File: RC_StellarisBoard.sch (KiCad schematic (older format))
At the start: 46 parts, among them K1 CONN_3, K2 CONN_3, K3 CONN_3, K4 CONN_3, K5 CONN_3, P1 CONN_2, P2 CONN_1, P3 CONN_1, P4 CONN_1, P5 CONN_1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

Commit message: buck boost, DCDC 5 done, servos done
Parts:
- removed D1: ZENER, ~, symbol ZENER
- removed Q1: MOSFET_P, ~, symbol MOSFET_P
- removed U3: NCP1117ST12T3G, ~, symbol NCP1117ST12T3G
- added C7: 22uF, ~, symbol C
- added L2: 2.2uH, ~, symbol INDUCTOR_SMALL
- added Q1: MOS_N, symbol MOS_N
- added R19: shunt, symbol R
- added U3: LM3668_DQB_12_SDF12A, symbol LM3668_DQB_12_SDF12A
- C4: value 1uF -> 10uF
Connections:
- wire segments 111 -> 122
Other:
- moved on the sheet: C4, R9

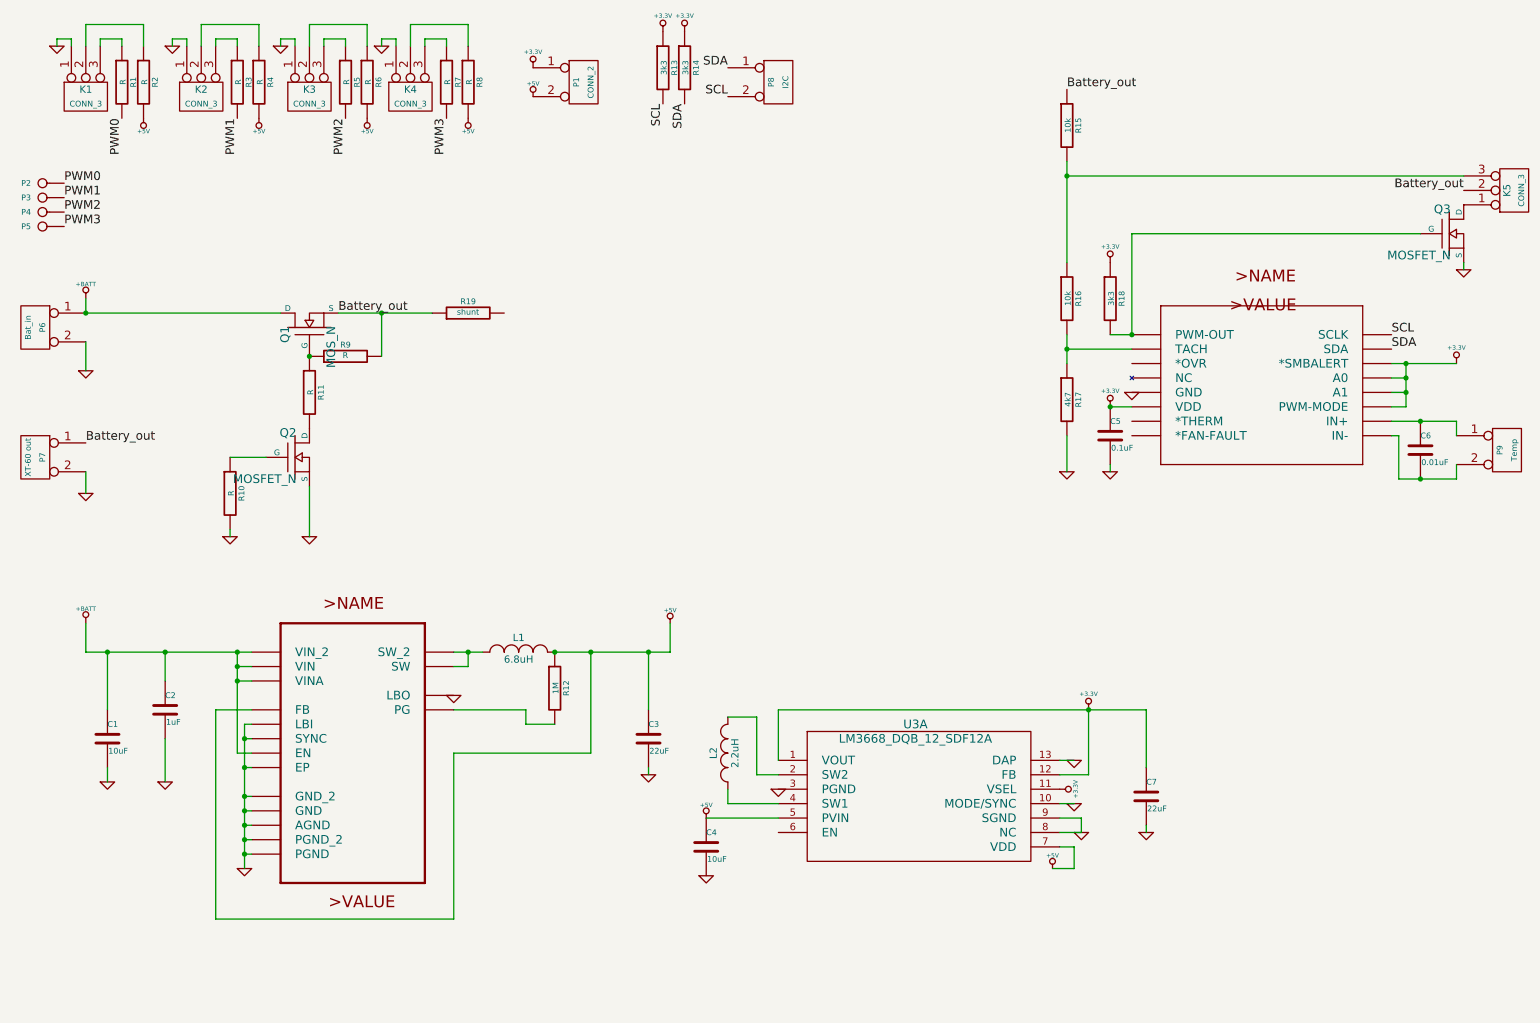
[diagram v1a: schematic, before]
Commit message: boost, mosfet + shunt
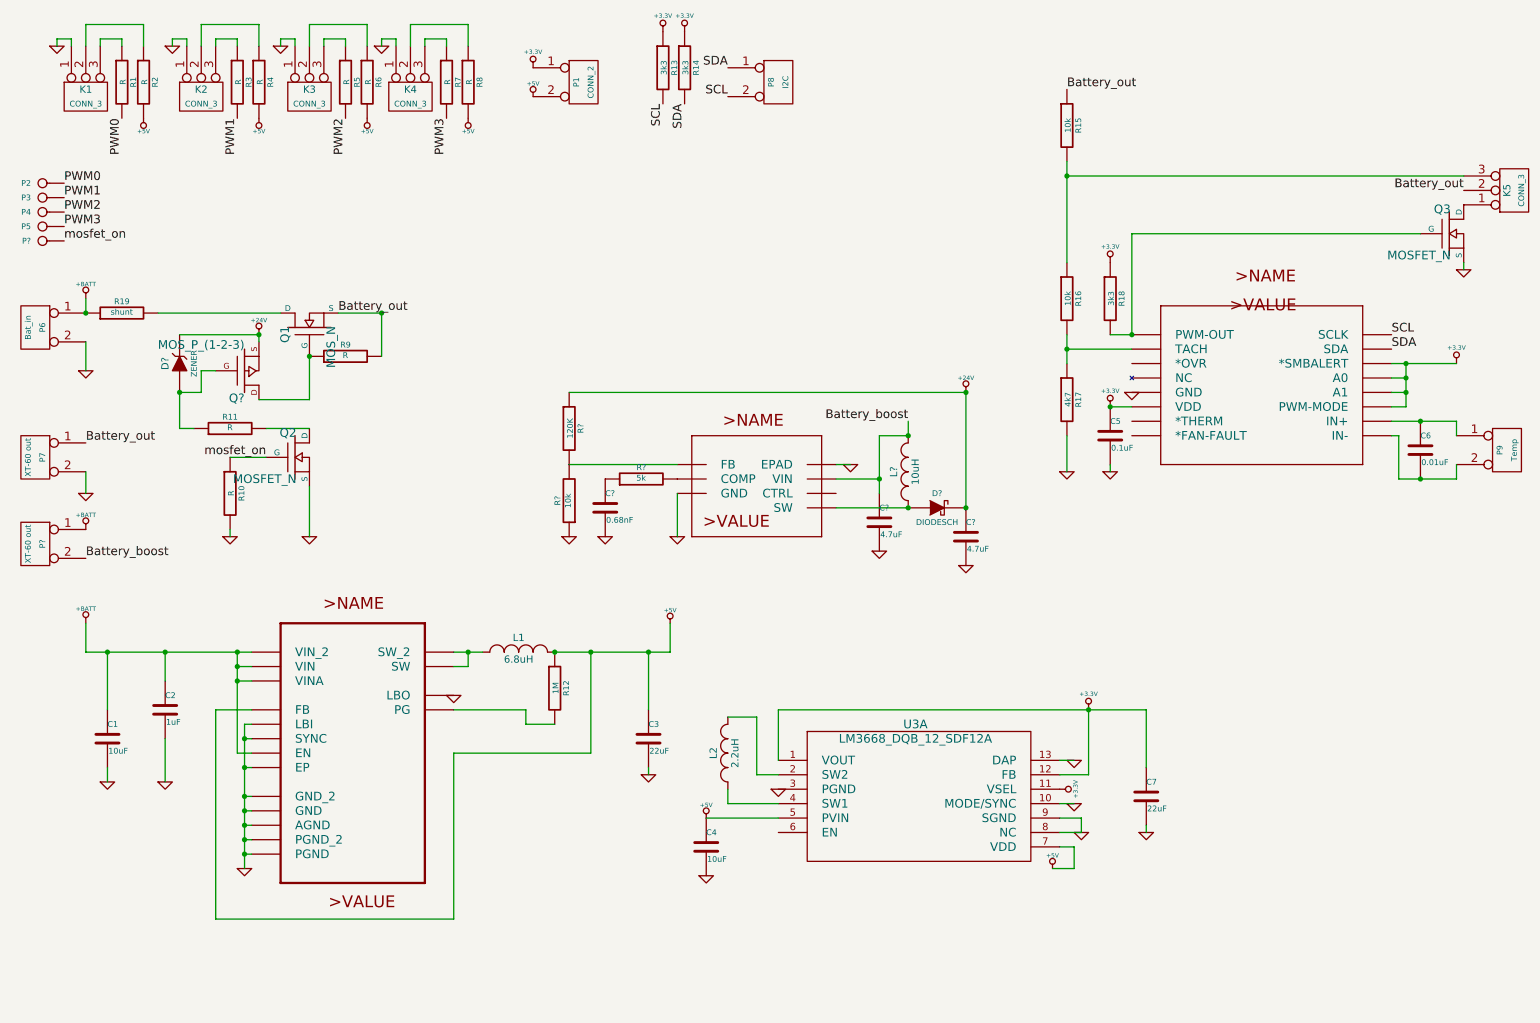
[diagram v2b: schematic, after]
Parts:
- added C?: 0.68nF, ~, symbol C
- added C? (x2): 4.7uF, ~, symbol C
- added D?: DIODESCH, ~, symbol DIODESCH
- added D?: ZENER, ~, symbol ZENER
- added L?: 10uH, ~, symbol INDUCTOR_SMALL
- added P?: XT-60 out, symbol CONN_2
- added P?: CONN_1, symbol CONN_1
- added Q?: MOS_P_(1-2-3), symbol MOS_P_(1-2-3)
- added R?: 5k, ~, symbol R
- added R?: 10k, ~, symbol R
- added R?: 120K, ~, symbol R
- added U?: TPS61170_DRV_6_DRV6_1P6X1, symbol TPS61170_DRV_6_DRV6_1P6X1
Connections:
- net +BATT: now also R19.1, P?.1 (P1); no longer Q1.D
- net Battery_out: no longer R19.1
- net GND: now also C?.2, C?.2, C?.2, R?.1, U?.3 (GND), U?.7 (EPAD)
- net mosfet_on: now reaches Q2.G, R10.1
- net mosfet_on: now also P?.1
- net at Q1.G, R9.1: now also Q?.D; no longer R11.1
- net at R19.2: now also Q1.D
- new net: D?.1 (A), Q?.G, R11.1
- new net: R?.2, R?.2, U?.1 (FB)
- new net: R?.2, U?.2 (COMP)
- new net: D?.1 (A), L?.1, U?.4 (SW)
- new net: C?.1, R?.1
- new net +24V: C?.1, D?.2 (K), D?.2 (K), Q?.S, R?.1
- new net Battery_boost: C?.1, L?.2, P?.2 (PM), U?.6 (VIN)
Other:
- moved on the sheet: R11, R19

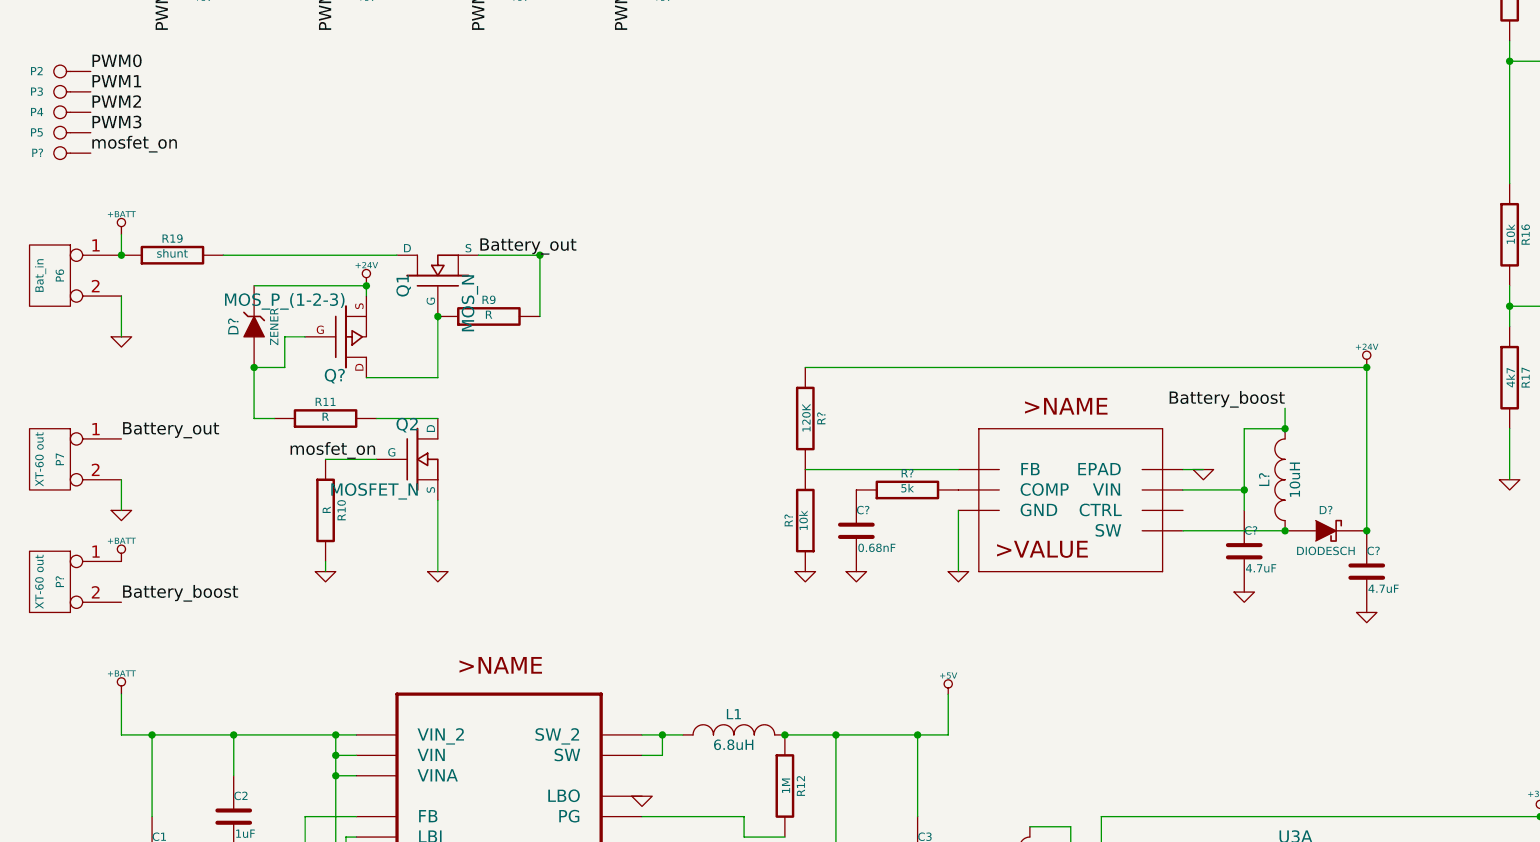
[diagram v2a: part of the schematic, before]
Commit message: falta footprints diodo
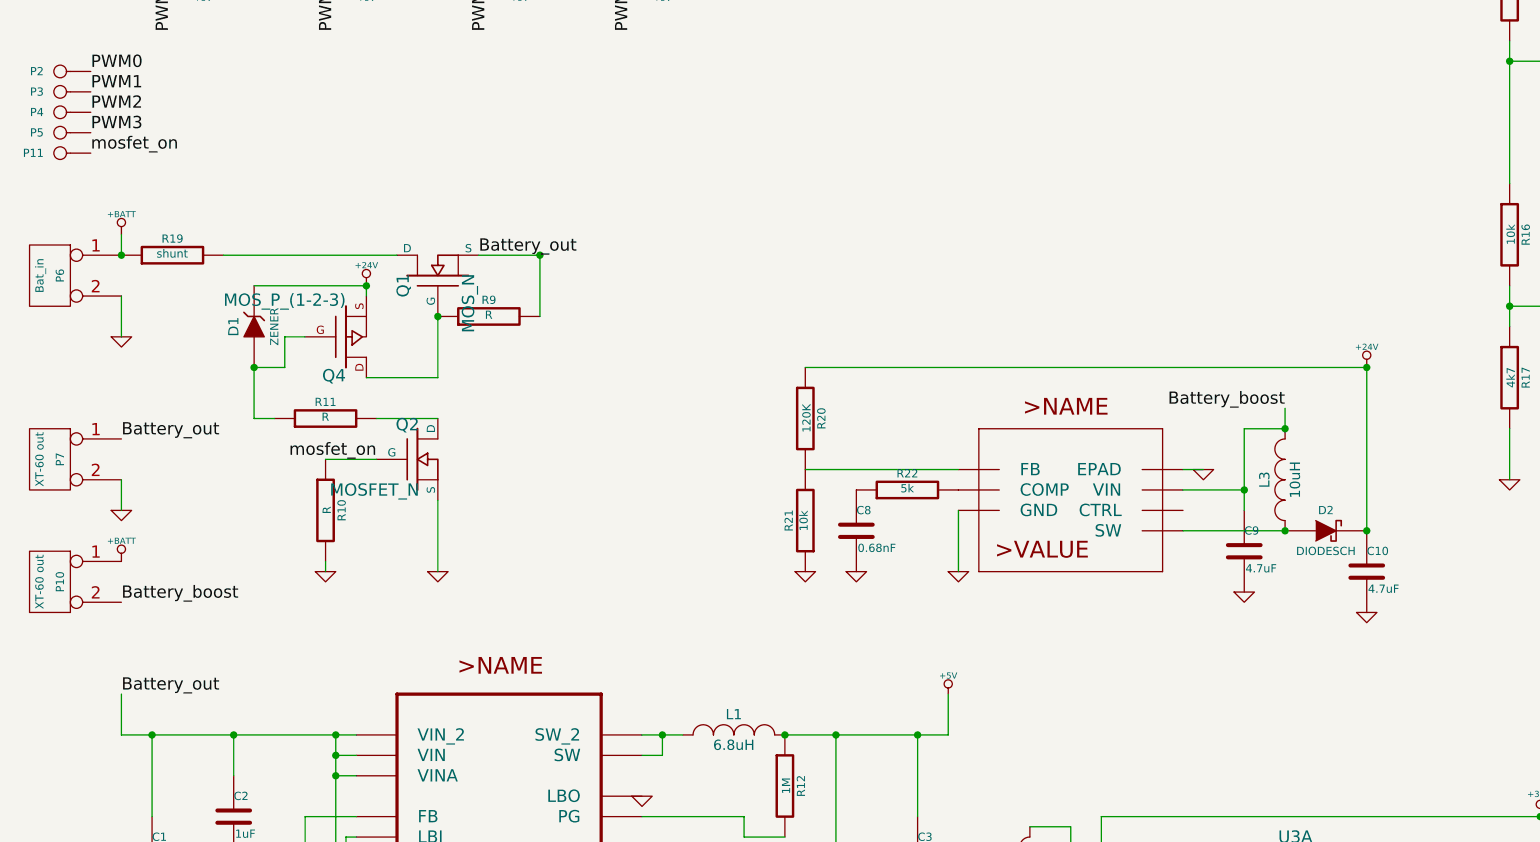
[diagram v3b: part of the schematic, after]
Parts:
- gave numbers to parts that had none: 13
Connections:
- net +BATT: no longer C1.1, C2.1, U2.2 (VIN_2), U2.3 (VIN), U2.4 (EN), U2.8 (VINA)
- net Battery_out: now also C1.1, C2.1, U2.2 (VIN_2), U2.3 (VIN), U2.4 (EN), U2.8 (VINA)
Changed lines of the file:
@@
 Sheet 1 1
 Title ""
-Date "6 jan 2014"
+Date "7 jan 2014"
 Rev ""
 Comp ""
@@
 	1100 2600 1100 2500
 Connection ~ 1100 2600
-$Comp
-L +BATT #PWR014
-U 1 1 52C981E3
-P 1100 4750
-F 0 "#PWR014" H 1100 4700 20  0001 C CNN
-F 1 "+BATT" H 1100 4850 30  0000 C CNN
-F 2 "" H 1100 4750 60  0000 C CNN
-F 3 "" H 1100 4750 60  0000 C CNN
-	1    1100 4750
-	1    0    0    -1
-$EndComp
 Wire Wire Line
 	1100 4750 1100 4950
@@
 $EndComp
 $Comp
-L TPS61170_DRV_6_DRV6_1P6X1 U?
+L TPS61170_DRV_6_DRV6_1P6X1 U4
 U 1 1 52CB3E20
 P 5700 3750
-F 0 "U?" H 5700 3750 0   0001 C CNN
+F 0 "U4" H 5700 3750 0   0001 C CNN
 F 1 "TPS61170_DRV_6_DRV6_1P6X1" H 5700 3750 0   0001 C CNN
 F 2 "" H 5700 3750 60  0000 C CNN
@@
 $EndComp
 $Comp
-L R R?
+L R R22
 U 1 1 52CB3E37
 P 4950 3750
-F 0 "R?" V 5030 3750 40  0000 C CNN
+F 0 "R22" V 5030 3750 40  0000 C CNN
 F 1 "5k" V 4957 3751 40  0000 C CNN
 F 2 "~" V 4880 3750 30  0000 C CNN
@@
 $EndComp
 $Comp
-L C C?
+L C C8
 U 1 1 52CB3E3D
 P 4700 3950
-F 0 "C?" H 4700 4050 40  0000 L CNN
+F 0 "C8" H 4700 4050 40  0000 L CNN
 F 1 "0.68nF" H 4706 3865 40  0000 L CNN
 F 2 "~" H 4738 3800 30  0000 C CNN
@@
 $EndComp
 $Comp
-L GND #PWR?
+L GND #PWR042
 U 1 1 52CB3E43
 P 4700 4150
-F 0 "#PWR?" H 4700 4150 30  0001 C CNN
+F 0 "#PWR042" H 4700 4150 30  0001 C CNN
 F 1 "GND" H 4700 4080 30  0001 C CNN
 F 2 "" H 4700 4150 60  0000 C CNN
@@
 $EndComp
 $Comp
-L GND #PWR?
+L GND #PWR043
 U 1 1 52CB3E49
 P 5200 4150
-F 0 "#PWR?" H 5200 4150 30  0001 C CNN
+F 0 "#PWR043" H 5200 4150 30  0001 C CNN
 F 1 "GND" H 5200 4080 30  0001 C CNN
 F 2 "" H 5200 4150 60  0000 C CNN
@@
 	5200 4150 5200 3850
 $Comp
-L R R?
+L R R21
 U 1 1 52CB3F80
 P 4450 3900
-F 0 "R?" V 4530 3900 40  0000 C CNN
+F 0 "R21" V 4530 3900 40  0000 C CNN
 F 1 "10k" V 4457 3901 40  0000 C CNN
 F 2 "~" V 4380 3900 30  0000 C CNN
@@
 $EndComp
 $Comp
-L R R?
+L R R20
 U 1 1 52CB3F86
 P 4450 3400
-F 0 "R?" V 4530 3400 40  0000 C CNN
+F 0 "R20" V 4530 3400 40  0000 C CNN
 F 1 "120K" V 4457 3401 40  0000 C CNN
 F 2 "~" V 4380 3400 30  0000 C CNN
@@
 	5200 3650 4450 3650
 $Comp
-L GND #PWR?
+L GND #PWR044
 U 1 1 52CB41F4
 P 4450 4150
-F 0 "#PWR?" H 4450 4150 30  0001 C CNN
+F 0 "#PWR044" H 4450 4150 30  0001 C CNN
 F 1 "GND" H 4450 4080 30  0001 C CNN
 F 2 "" H 4450 4150 60  0000 C CNN
@@
 $EndComp
 $Comp
-L GND #PWR?
+L GND #PWR045
 U 1 1 52CB41FA
 P 6400 3650
-F 0 "#PWR?" H 6400 3650 30  0001 C CNN
+F 0 "#PWR045" H 6400 3650 30  0001 C CNN
 F 1 "GND" H 6400 3580 30  0001 C CNN
 F 2 "" H 6400 3650 60  0000 C CNN
@@
 	6400 3650 6300 3650
 $Comp
-L INDUCTOR_SMALL L?
+L INDUCTOR_SMALL L3
 U 1 1 52CB4337
 P 6800 3700
-F 0 "L?" H 6800 3800 50  0000 C CNN
+F 0 "L3" H 6800 3800 50  0000 C CNN
 F 1 "10uH" H 6800 3650 50  0000 C CNN
 F 2 "~" H 6800 3700 60  0000 C CNN
@@
 $EndComp
 $Comp
-L C C?
+L C C10
 U 1 1 52CB433D
 P 7200 4150
-F 0 "C?" H 7200 4250 40  0000 L CNN
+F 0 "C10" H 7200 4250 40  0000 L CNN
 F 1 "4.7uF" H 7206 4065 40  0000 L CNN
 F 2 "~" H 7238 4000 30  0000 C CNN
@@
 $EndComp
 $Comp
-L DIODESCH D?
+L DIODESCH D2
 U 1 1 52CB4345
 P 7000 3950
-F 0 "D?" H 7000 4050 40  0000 C CNN
+F 0 "D2" H 7000 4050 40  0000 C CNN
 F 1 "DIODESCH" H 7000 3850 40  0000 C CNN
 F 2 "~" H 7000 3950 60  0000 C CNN
@@
 Connection ~ 6600 3750
 $Comp
-L C C?
+L C C9
 U 1 1 52CB45F5
 P 6600 4050
-F 0 "C?" H 6600 4150 40  0000 L CNN
+F 0 "C9" H 6600 4150 40  0000 L CNN
 F 1 "4.7uF" H 6606 3965 40  0000 L CNN
 F 2 "~" H 6638 3900 30  0000 C CNN
@@
 $EndComp
 $Comp
-L GND #PWR?
+L GND #PWR046
 U 1 1 52CB45FB
 P 6600 4250
-F 0 "#PWR?" H 6600 4250 30  0001 C CNN
+F 0 "#PWR046" H 6600 4250 30  0001 C CNN
 F 1 "GND" H 6600 4180 30  0001 C CNN
 F 2 "" H 6600 4250 60  0000 C CNN
@@
 $EndComp
 $Comp
-L GND #PWR?
+L GND #PWR047
 U 1 1 52CB4601
 P 7200 4350
-F 0 "#PWR?" H 7200 4350 30  0001 C CNN
+F 0 "#PWR047" H 7200 4350 30  0001 C CNN
 F 1 "GND" H 7200 4280 30  0001 C CNN
 F 2 "" H 7200 4350 60  0000 C CNN
@@
 Connection ~ 7200 3950
 $Comp
-L +BATT #PWR?
+L +BATT #PWR048
 U 1 1 52CB4753
 P 1100 4100
-F 0 "#PWR?" H 1100 4050 20  0001 C CNN
+F 0 "#PWR048" H 1100 4050 20  0001 C CNN
 F 1 "+BATT" H 1100 4200 30  0000 C CNN
 F 2 "" H 1100 4100 60  0000 C CNN
@@
 Battery_boost
 $Comp
-L CONN_2 P?
+L CONN_2 P10
 U 1 1 52CB475B
 P 750 4200
-F 0 "P?" V 700 4200 40  0000 C CNN
+F 0 "P10" V 700 4200 40  0000 C CNN
 F 1 "XT-60 out" V 800 4200 40  0000 C CNN
 F 2 "" H 750 4200 60  0000 C CNN
@@
 Connection ~ 6800 3450
 $Comp
-L +24V #PWR?
+L +24V #PWR049
 U 1 1 52CB4830
 P 7200 3150
-F 0 "#PWR?" H 7200 3100 20  0001 C CNN
+F 0 "#PWR049" H 7200 3100 20  0001 C CNN
 F 1 "+24V" H 7200 3250 30  0000 C CNN
 F 2 "" H 7200 3150 60  0000 C CNN
@@
 Connection ~ 7200 3150
 $Comp
-L MOS_P_(1-2-3) Q?
+L MOS_P_(1-2-3) Q4
 U 1 1 52CB4853
 P 2200 3000
-F 0 "Q?" H 2200 3190 60  0000 R CNN
+F 0 "Q4" H 2200 3190 60  0000 R CNN
 F 1 "MOS_P_(1-2-3)" H 2200 2820 60  0000 R CNN
 F 2 "" H 2200 3000 60  0000 C CNN
@@
 $EndComp
 $Comp
-L ZENER D?
+L ZENER D1
 U 1 1 52CB4919
 P 1750 2950
-F 0 "D?" H 1750 3050 50  0000 C CNN
+F 0 "D1" H 1750 3050 50  0000 C CNN
 F 1 "ZENER" H 1750 2850 40  0000 C CNN
 F 2 "~" H 1750 2950 60  0000 C CNN
@@
 $EndComp
 $Comp
-L +24V #PWR?
+L +24V #PWR050
 U 1 1 52CB4930
 P 2300 2750
-F 0 "#PWR?" H 2300 2700 20  0001 C CNN
+F 0 "#PWR050" H 2300 2700 20  0001 C CNN
 F 1 "+24V" H 2300 2850 30  0000 C CNN
 F 2 "" H 2300 2750 60  0000 C CNN
@@
 	2650 3200 2650 2900
 $Comp
-L CONN_1 P?
+L CONN_1 P11
 U 1 1 52CB4D3F
 P 800 2100
-F 0 "P?" H 880 2100 40  0000 L CNN
+F 0 "P11" H 880 2100 40  0000 L CNN
 F 1 "CONN_1" H 800 2155 30  0001 C CNN
 F 2 "" H 800 2100 60  0000 C CNN
@@
 Wire Wire Line
 	3150 2600 2850 2600
+Text Label 1100 4750 0    60   ~ 0
+Battery_out
 $EndSCHEMATC
